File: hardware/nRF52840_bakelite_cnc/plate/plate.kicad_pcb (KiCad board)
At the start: 2 copper layers, 299.2 x 122.8 mm, 88 parts

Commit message: M  hardware/nRF52840_bakelite_cnc/border.py M  hardware/nRF52840_bakelite_cnc/pcb/pcb.kicad_prl M  hardware/nRF52840_bakelite_cnc/plate/plate.kicad_pcb M  hardware/nRF52840_bakelite_cnc/plate/plate.kicad_sch M  hardware/nRF52840_bakelite_cnc/plate/sym-lib-table
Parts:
- removed Hs11, Hs12: MountingHole, MountingHole:MountingHole_2.1mm
- S42, S70: footprint tmr-lib:Switch_Cutout_1.25u -> tmr-lib:Switch_Cutout
- S46: footprint tmr-lib:Switch_Cutout_1.75u -> tmr-lib:Switch_Cutout
- S57: footprint tmr-lib:Switch_Cutout_1.75u -> tmr-lib:Switch_Cutout_1.25u
- moved JLC1 222.5 mm to (268.1, 19.5), turned to -90 degrees
- moved Hs9 114.0 mm to (209.0, 27.9)
- moved Hs8 109.4 mm to (95.0, 27.9)
- moved Hs7 102.8 mm to (189.1, 83.6)
- moved Hs5 95.0 mm to (137.8, 46.9)
- moved Hs10 66.7 mm to (264.8, 64.6)
- moved Hs6 63.1 mm to (86.4, 83.6)
- moved Hs4 26.0 mm to (25.0, 61.0)
- moved BAT2 23.4 mm to (243.4, 61.0), turned to 180 degrees
- moved S58 9.50 mm to (275.5, 57.0)
- moved Jusb1 5.46 mm to (20.8, -13.4)
- moved S72 5.35 mm to (275.5, 76.0)
- moved S71 5.22 mm to (256.6, 76.0)
- moved S43 4.75 mm to (261.2, 38.0)
- moved S44 4.75 mm to (280.2, 38.0)
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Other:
- board size 299.2 x 122.8 mm -> 294.5 x 122.8 mm

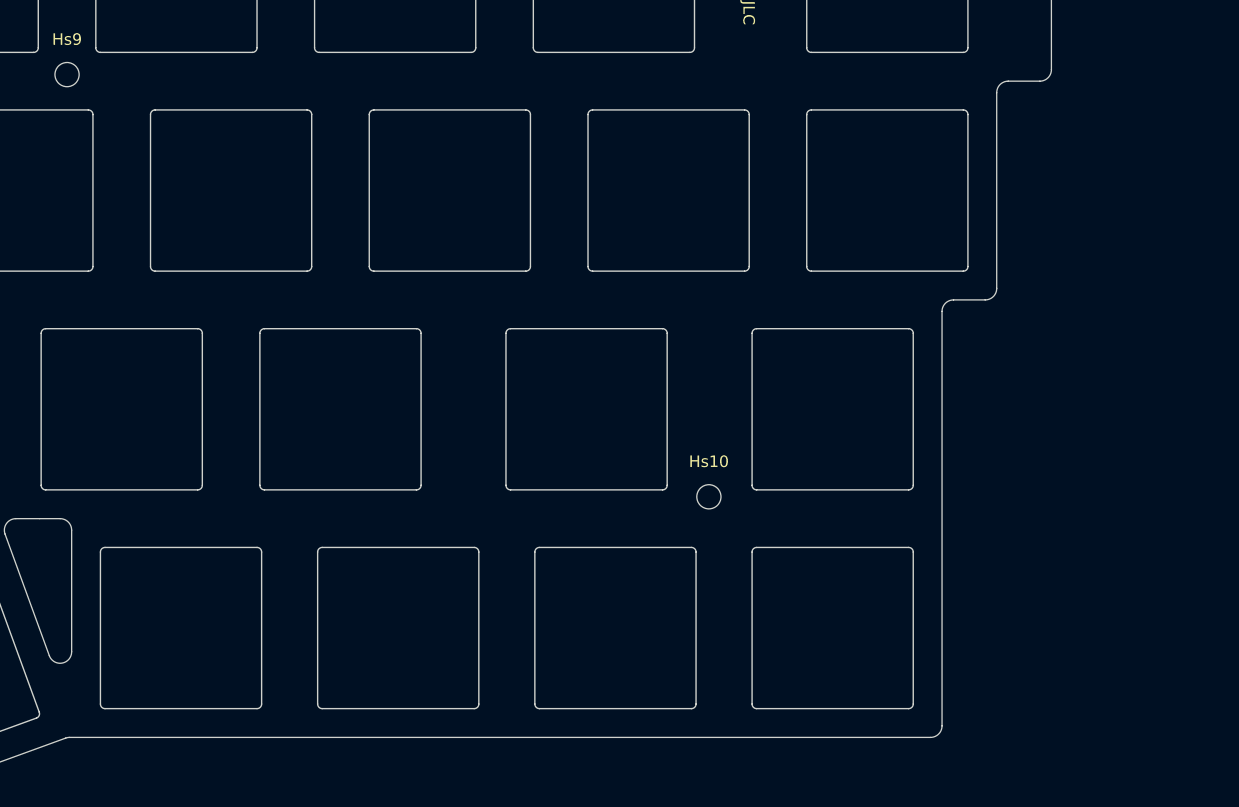
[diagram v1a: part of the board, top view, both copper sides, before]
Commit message: M  hardware/nRF52840_bakelite_cnc/border.py M  hardware/nRF52840_bakelite_cnc/pcb/pcb.kicad_pcb M  hardware/nRF52840_bakelite_cnc/pcb/pcb.kicad_prl M  hardware/nRF52840_bakelite_cnc/pcb/pcb.kicad_pro M  hardware/nRF52840_bakelite_cnc/pcb/pcb.kicad_sch M  hardware/nRF52840_bakelite_cnc/pcb/switch.kicad_sch M  hardware/nRF52840_bakelite_cnc/placefp.py M  hardware/nRF52840_bakelite_cnc/plate/plate.kicad_pcb M  hardware/nRF52840_bakelite_cnc/plate/plate.kicad_sch A  hardware/nRF52840_bakelite_cnc/tmr-footprints/C_0402_1005Metric_Cvcc.kicad_mod A  hardware/nRF52840_bakelite_cnc/tmr-footprints/C_0402_1005Metric_Cvout.kicad_mod M  hardware/nRF52840_bakelite_cnc/tmr-footprints/Gateron_Switch_Lowpro.kicad_mod A  hardware/nRF52840_bakelite_cnc/tmr-footprints/PCB_Wire_Solder_3p_Connector.kicad_mod
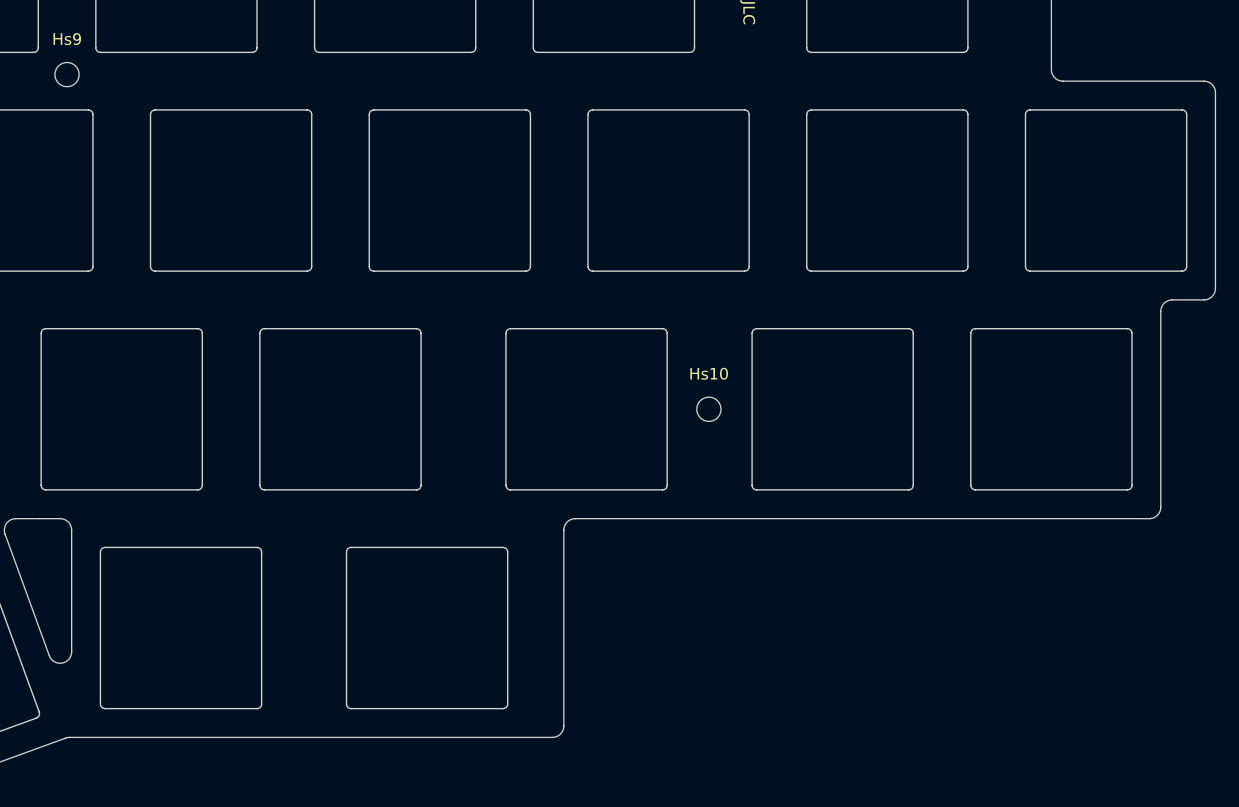
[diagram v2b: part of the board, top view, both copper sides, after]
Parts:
- S70: footprint tmr-lib:Switch_Cutout -> tmr-lib:Switch_Cutout_1.25u
- moved S72 44.8 mm to (299.2, 38.0)
- moved S71 42.4 mm to (294.5, 57.0)
- moved Hs10 7.60 mm to (264.8, 57.0)
- moved BAT1 4.00 mm to (23.6, 80.0), turned to 0 degrees
- moved S70 2.51 mm to (240.3, 76.0)
- moved BAT2 2.00 mm to (243.5, 63.0), turned to 0 degrees
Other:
- board size 294.5 x 122.8 mm -> 308.8 x 122.8 mm
